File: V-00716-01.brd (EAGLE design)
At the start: 57 x 33 mm, 23 parts, among them Q1 16MHz, U1 ATMEGA32-16AU, X1 MINI-USB-32005-201

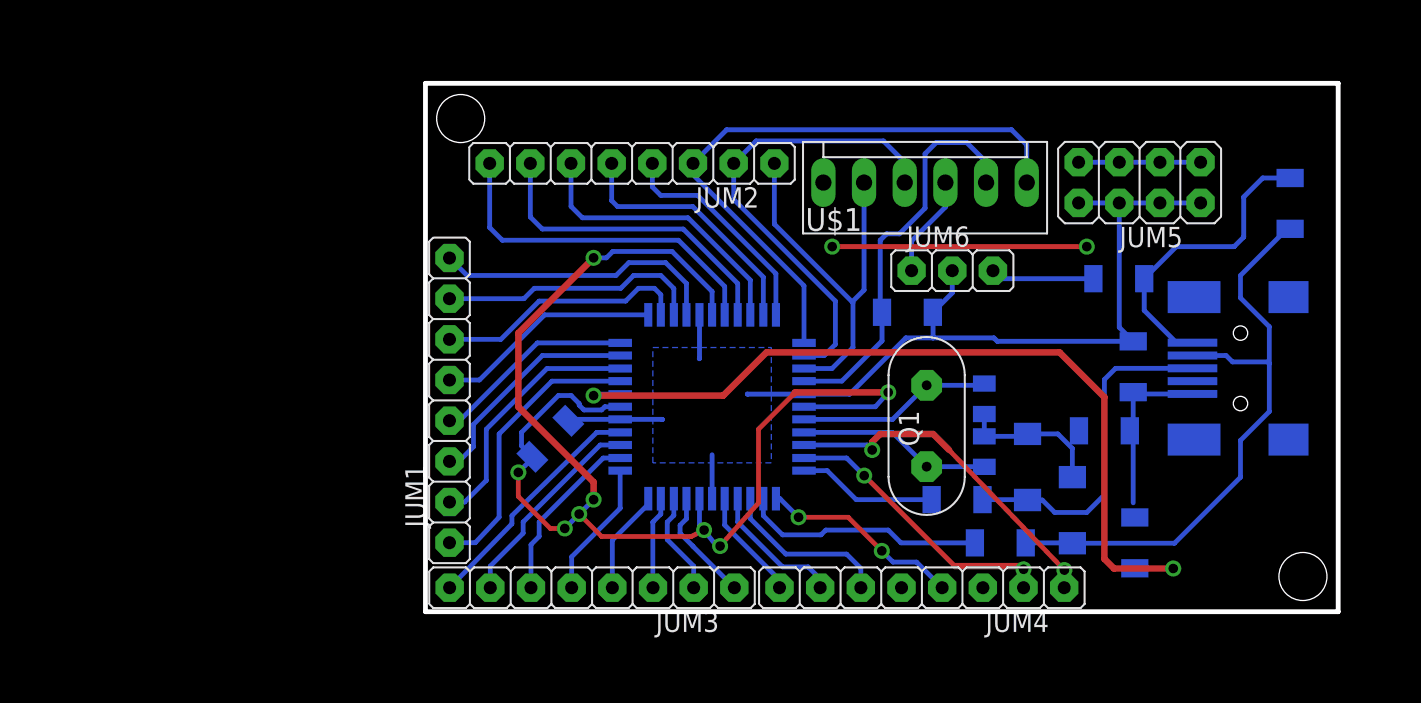
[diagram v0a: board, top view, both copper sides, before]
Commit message: v1.1.0.2
Uprava pro vyrobu v Gatemě
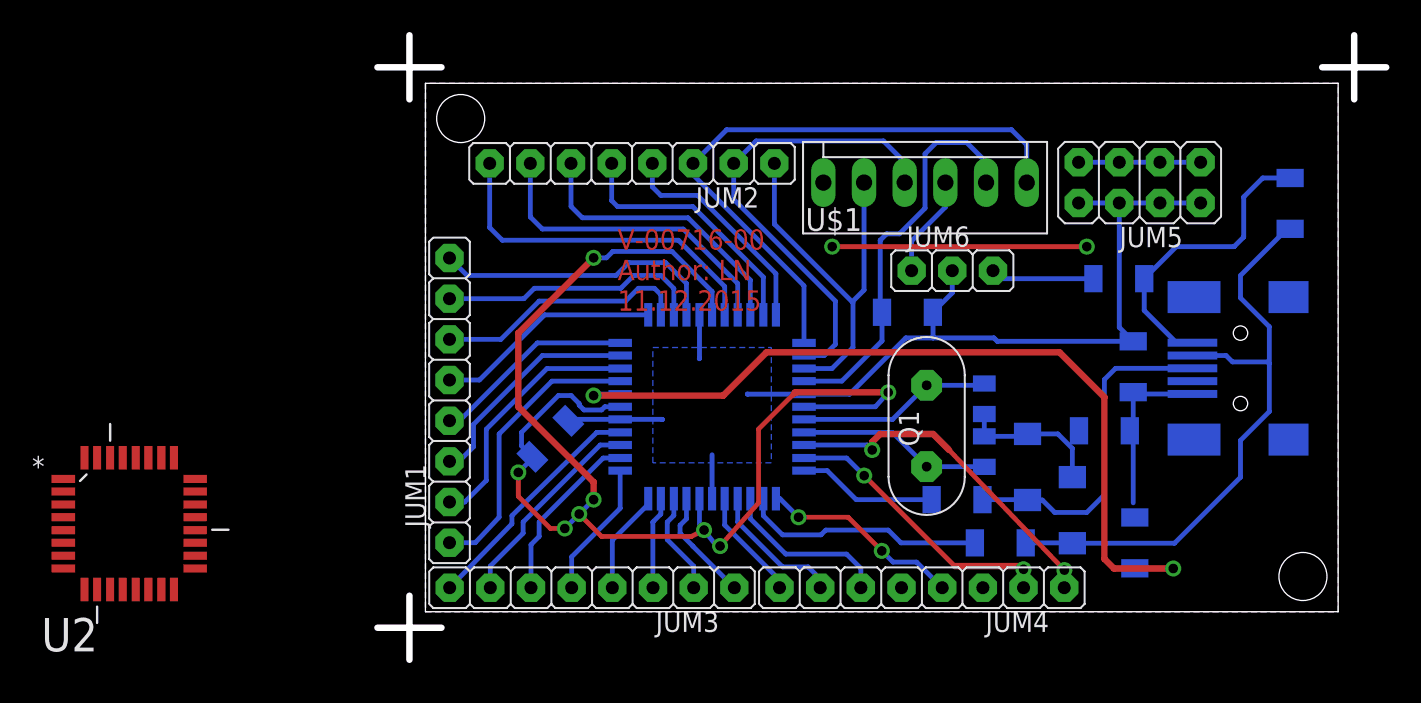
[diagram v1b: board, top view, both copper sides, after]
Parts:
- added U2: ATMEGA32U2-AU, #_Atmel_By_element14_Batch_1-00:QFP80P900X900X120-32N
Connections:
- new net N$12: U2.27
- new net N$13: U2.32
- new net N$2: U2.1
- new net N$28: U2.4
- new net N$3: U2.2
- new net N$31: U2.3
- new net N$32: U2.28
- net DATA+: now also U2.29
- net DATA-: now also U2.30
- net VCCINT: now also U2.31
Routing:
- added copper zone on layer 1, net GNDINT
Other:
- board size 57 x 33 mm -> 63 x 39 mm
- board text added: "V-00716-00 Author: LN 11.12.2015"
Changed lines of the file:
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@@
 <layer number="37" name="tTest" color="7" fill="1" visible="no" active="yes"/>
 <layer number="38" name="bTest" color="7" fill="1" visible="no" active="yes"/>
-<layer number="39" name="tKeepout" color="4" fill="11" visible="yes" active="yes"/>
-<layer number="40" name="bKeepout" color="1" fill="11" visible="yes" active="yes"/>
-<layer number="41" name="tRestrict" color="4" fill="10" visible="yes" active="yes"/>
-<layer number="42" name="bRestrict" color="1" fill="10" visible="yes" active="yes"/>
-<layer number="43" name="vRestrict" color="2" fill="10" visible="yes" active="yes"/>
+<layer number="39" name="tKeepout" color="4" fill="11" visible="no" active="yes"/>
+<layer number="40" name="bKeepout" color="1" fill="11" visible="no" active="yes"/>
+<layer number="41" name="tRestrict" color="4" fill="10" visible="no" active="yes"/>
+<layer number="42" name="bRestrict" color="1" fill="10" visible="no" active="yes"/>
+<layer number="43" name="vRestrict" color="2" fill="10" visible="no" active="yes"/>
 <layer number="44" name="Drills" color="7" fill="1" visible="no" active="yes"/>
-<layer number="45" name="Holes" color="7" fill="1" visible="yes" active="yes"/>
+<layer number="45" name="Holes" color="7" fill="1" visible="no" active="yes"/>
 <layer number="46" name="Milling" color="3" fill="1" visible="no" active="yes"/>
-<layer number="47" name="Measures" color="7" fill="1" visible="yes" active="yes"/>
-<layer number="48" name="Document" color="7" fill="1" visible="yes" active="yes"/>
-<layer number="49" name="Reference" color="7" fill="1" visible="yes" active="yes"/>
-<layer number="50" name="dxf" color="7" fill="1" visible="yes" active="yes"/>
-<layer number="51" name="tDocu" color="7" fill="1" visible="yes" active="yes"/>
-<layer number="52" name="bDocu" color="7" fill="1" visible="yes" active="yes"/>
+<layer number="47" name="Measures" color="7" fill="1" visible="no" active="yes"/>
+<layer number="48" name="Document" color="7" fill="1" visible="no" active="yes"/>
+<layer number="49" name="Reference" color="7" fill="1" visible="no" active="yes"/>
+<layer number="50" name="dxf" color="7" fill="1" visible="no" active="yes"/>
+<layer number="51" name="tDocu" color="7" fill="1" visible="no" active="yes"/>
+<layer number="52" name="bDocu" color="7" fill="1" visible="no" active="yes"/>
 <layer number="53" name="tGND_GNDA" color="7" fill="1" visible="no" active="no"/>
 <layer number="54" name="bGND_GNDA" color="7" fill="1" visible="no" active="no"/>
@@
 <layer number="97" name="Info" color="7" fill="1" visible="no" active="no"/>
 <layer number="98" name="Guide" color="6" fill="1" visible="no" active="no"/>
-<layer number="100" name="PaJa" color="12" fill="7" visible="yes" active="yes"/>
-<layer number="101" name="Doplnky" color="5" fill="1" visible="yes" active="yes"/>
-<layer number="102" name="Kola" color="11" fill="7" visible="yes" active="yes"/>
-<layer number="103" name="Popisy" color="7" fill="1" visible="yes" active="yes"/>
-<layer number="104" name="Zapojeni" color="7" fill="1" visible="yes" active="yes"/>
-<layer number="105" name="tPlate" color="7" fill="1" visible="yes" active="yes"/>
-<layer number="106" name="bPlate" color="7" fill="1" visible="yes" active="yes"/>
+<layer number="100" name="PaJa" color="12" fill="7" visible="no" active="yes"/>
+<layer number="101" name="Doplnky" color="5" fill="1" visible="no" active="yes"/>
+<layer number="102" name="Kola" color="11" fill="7" visible="no" active="yes"/>
+<layer number="103" name="Popisy" color="7" fill="1" visible="no" active="yes"/>
+<layer number="104" name="Zapojeni" color="7" fill="1" visible="no" active="yes"/>
+<layer number="105" name="tPlate" color="7" fill="1" visible="no" active="yes"/>
+<layer number="106" name="bPlate" color="7" fill="1" visible="no" active="yes"/>
 <layer number="107" name="Crop" color="7" fill="1" visible="no" active="no"/>
-<layer number="110" name="wago-seda" color="7" fill="8" visible="yes" active="yes"/>
-<layer number="111" name="wago-cervena" color="12" fill="8" visible="yes" active="yes"/>
-<layer number="112" name="wago-zelena" color="2" fill="8" visible="yes" active="yes"/>
-<layer number="113" name="wago-modra" color="1" fill="8" visible="yes" active="yes"/>
+<layer number="110" name="wago-seda" color="7" fill="8" visible="no" active="yes"/>
+<layer number="111" name="wago-cervena" color="12" fill="8" visible="no" active="yes"/>
+<layer number="112" name="wago-zelena" color="2" fill="8" visible="no" active="yes"/>
+<layer number="113" name="wago-modra" color="1" fill="8" visible="no" active="yes"/>
 <layer number="116" name="centerDrill" color="7" fill="1" visible="yes" active="yes"/>
 <layer number="121" name="_tsilk" color="7" fill="1" visible="no" active="no"/>
@@
 <board>
 <plain>
-<wire x1="0" y1="0" x2="57" y2="0" width="0.3" layer="20"/>
-<wire x1="57" y1="0" x2="57" y2="33" width="0.3" layer="20"/>
-<wire x1="57" y1="33" x2="0" y2="33" width="0.3" layer="20"/>
-<wire x1="0" y1="33" x2="0" y2="0" width="0.3" layer="20"/>
+<wire x1="0" y1="0" x2="57" y2="0" width="0" layer="20"/>
+<wire x1="57" y1="0" x2="57" y2="33" width="0" layer="20"/>
+<wire x1="57" y1="33" x2="0" y2="33" width="0" layer="20"/>
+<wire x1="0" y1="33" x2="0" y2="0" width="0" layer="20"/>
 <dimension x1="0" y1="33" x2="0" y2="0" x3="-6.8" y3="16.5" textsize="1.778" layer="47"/>
 <dimension x1="57" y1="33" x2="0" y2="33" x3="28.5" y3="36.8" textsize="1.778" layer="47"/>
 <hole x="2.2" y="30.8" drill="3"/>
 <hole x="54.8" y="2.2" drill="3"/>
+<text x="12" y="18.8" size="1.27" layer="1" font="vector" ratio="20">V-00716-00
+Author: LN
+11.12.2015</text>
+<wire x1="1" y1="-1" x2="-1" y2="-1" width="0.4064" layer="20"/>
+<wire x1="-1" y1="-1" x2="-3" y2="-1" width="0.4064" layer="20"/>
+<wire x1="-1" y1="-1" x2="-1" y2="1" width="0.4064" layer="20"/>
+<wire x1="-1" y1="-1" x2="-1" y2="-3" width="0.4064" layer="20"/>
+<wire x1="-1" y1="34" x2="-1" y2="32" width="0.4064" layer="20"/>
+<wire x1="-1" y1="34" x2="1" y2="34" width="0.4064" layer="20"/>
+<wire x1="-1" y1="34" x2="-3" y2="34" width="0.4064" layer="20"/>
+<wire x1="-1" y1="34" x2="-1" y2="36" width="0.4064" layer="20"/>
+<wire x1="58" y1="34" x2="58" y2="32" width="0.4064" layer="20"/>
+<wire x1="58" y1="34" x2="56" y2="34" width="0.4064" layer="20"/>
+<wire x1="58" y1="34" x2="60" y2="34" width="0.4064" layer="20"/>
+<wire x1="58" y1="34" x2="58" y2="36" width="0.4064" layer="20"/>
 </plain>
 <attributes>
@@
 <element name="JUM6" library="#PaJa_konektory" package="S1G3_JUM" value="S1G3_JUMP" x="32.9" y="21.3"/>
 <element name="R6" library="#PaJa_31" package="1206" value="0R" x="43.3" y="20.8" rot="MR180"/>
+<element name="U2" library="#_Atmel_By_element14_Batch_1-00" package="QFP80P900X900X120-32N" value="ATMEGA32U2-AU" x="-18.5" y="5.5">
+<attribute name="PACKAGE" value="TQFP-32" x="-18.5" y="5.5" size="1.778" layer="27" display="off"/>
+<attribute name="OC_NEWARK" value="26R5632" x="-18.5" y="5.5" size="1.778" layer="27" display="off"/>
+<attribute name="MPN" value="ATMEGA32U2-AU" x="-18.5" y="5.5" size="1.778" layer="27" display="off"/>
+<attribute name="SUPPLIER" value="Atmel" x="-18.5" y="5.5" size="1.778" layer="27" display="off"/>
+<attribute name="OC_FARNELL" value="1748524" x="-18.5" y="5.5" size="1.778" layer="27" display="off"/>
+</element>
 </elements>
 <signals>
@@
 <wire x1="51.1" y1="25.9" x2="52.2875" y2="27.0875" width="0.3048" layer="16"/>
 <wire x1="52.2875" y1="27.0875" x2="54" y2="27.0875" width="0.3048" layer="16"/>
+<contactref element="U2" pad="31"/>
 <wire x1="41.7125" y1="20.8" x2="44.8875" y2="20.8" width="0" layer="19" extent="16-16"/>
+<wire x1="-20.5066" y1="9.6148" x2="35.44" y2="21.3" width="0" layer="19" extent="1-1"/>
 </signal>
 <signal name="DATA-">
@@
 <wire x1="54" y1="23.9125" x2="53.8125" y2="23.9125" width="0.3048" layer="16"/>
 <wire x1="53.8125" y1="23.9125" x2="50.9" y2="21" width="0.3048" layer="16"/>
+<contactref element="U2" pad="30"/>
+<wire x1="-19.6938" y1="9.6148" x2="37.4875" y2="4.3" width="0" layer="19" extent="1-16"/>
 </signal>
 <signal name="DATA+">
@@
 <wire x1="41.3" y1="6.2" x2="42.4" y2="7.3" width="0.3" layer="16"/>
 <wire x1="42.4" y1="7.3" x2="42.4" y2="14.5" width="0.3" layer="16"/>
+<contactref element="U2" pad="29"/>
+<wire x1="-18.9064" y1="9.6148" x2="34.7875" y2="7" width="0" layer="19" extent="1-16"/>
 </signal>
 <signal name="N.C.">
@@
 <wire x1="28.9" y1="13.7" x2="23.1" y2="13.7" width="0.4064" layer="1"/>
 <wire x1="23.1" y1="13.7" x2="23" y2="13.6" width="0.4064" layer="1"/>
+<polygon width="0.3" layer="1" isolate="0.4064" rank="6">
+<vertex x="0" y="0"/>
+<vertex x="57" y="0"/>
+<vertex x="57" y="33"/>
+<vertex x="0" y="33"/>
+</polygon>
+<polygon width="0.3" layer="16" isolate="0.4064" rank="6">
+<vertex x="0" y="0"/>
+<vertex x="57" y="0"/>
+<vertex x="57" y="33"/>
+<vertex x="0" y="33"/>
+</polygon>
 <wire x1="43.9875" y1="11.3" x2="40.8125" y2="11.3" width="0" layer="19" extent="16-16"/>
-<wire x1="25.4" y1="22.8" x2="17.9" y2="20" width="0" layer="19" extent="16-16"/>
 </signal>
 <signal name="PD2">
@@
 <wire x1="32.9" y1="19.9125" x2="32.9" y2="21.3" width="0.3048" layer="16"/>
 </signal>
+<signal name="N$2">
+<contactref element="U2" pad="1"/>
+</signal>
+<signal name="N$3">
+<contactref element="U2" pad="2"/>
+</signal>
+<signal name="N$12">
+<contactref element="U2" pad="27"/>
+</signal>
+<signal name="N$13">
+<contactref element="U2" pad="32"/>
+</signal>
+<signal name="N$28">
+<contactref element="U2" pad="4"/>
+</signal>
+<signal name="N$31">
+<contactref element="U2" pad="3"/>
+</signal>
+<signal name="N$32">
+<contactref element="U2" pad="28"/>
+</signal>
 </signals>
 <errors>
@@
 </board>
 </drawing>
+<compatibility>
+<note version="6.3" minversion="6.2.2" severity="warning">
+Since Version 6.2.2 text objects can contain more than one line,
+which will not be processed correctly with this version.
+</note>
+</compatibility>
 </eagle>
